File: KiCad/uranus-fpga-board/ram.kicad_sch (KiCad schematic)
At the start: 61 parts, among them U6 AS4C256M16D3, U7 AS4C256M16D3, U8 AS4C256M16D3, U9 AS4C256M16D3

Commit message: New entry and schematic
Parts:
- added Y1: SX7DF200.000B20F30DNN, Oscillator:Oscillator_SMD_IDT_JU6-6_7.0x5.0mm_P2.54mm, symbol Oscillator:XUX71
- C10: renamed from C1; value 100 nF -> 100 nF 0.1%
- C11: renamed from C2; value 100 nF -> 100 nF 0.1%
- C13: renamed from C28; value C_Small -> 100 nF
- C14: renamed from C29; value C_Small -> 100 nF
- C15: renamed from C30; value C_Small -> 100 nF
- C16: renamed from C31; value C_Small -> 100 nF
- C17: renamed from C32; value C_Small -> 100 nF
- C18: renamed from C33; value C_Small -> 100 nF
- C19: renamed from C34; value C_Small -> 100 nF
- C2: renamed from C10; value C_Small -> 100 nF
- C20: renamed from C35; value C_Small -> 100 nF
- C21: renamed from C5; value 100 nF -> 100 nF 0.1%
- C23: renamed from C19; value C_Small -> 100 nF
- C24: renamed from C20; value C_Small -> 100 nF
- C25: renamed from C21; value C_Small -> 100 nF
- C26: renamed from C22; value C_Small -> 100 nF
- C27: renamed from C23; value C_Small -> 100 nF
- C28: renamed from C24; value C_Small -> 100 nF
- C29: renamed from C25; value C_Small -> 100 nF
- C3: renamed from C11; value C_Small -> 100 nF
- C30: renamed from C26; value C_Small -> 100 nF
- C31: renamed from C6; value 100 nF -> 100 nF 0.1%
- C33: renamed from C37; value C_Small -> 100 nF
- C34: renamed from C38; value C_Small -> 100 nF
- C35: renamed from C39; value C_Small -> 100 nF
- C36: renamed from C40; value C_Small -> 100 nF
- C37: renamed from C41; value C_Small -> 100 nF
- C38: renamed from C42; value C_Small -> 100 nF
- C39: renamed from C43; value C_Small -> 100 nF
- C4: renamed from C12; value C_Small -> 100 nF
- C40: renamed from C44; value C_Small -> 100 nF
- C41: renamed from C7; value 100 nF -> 100 nF 0.1%
- C42: renamed from C8; value 100 nF -> 100 nF 0.1%
- C43: renamed from C45; value 10 uF -> 10 μF
- C44: renamed from C3; value 100 nF -> 100 nF 0.1%
- C45: renamed from C4; value 100 nF -> 100 nF 0.1%
- C5: renamed from C13; value C_Small -> 100 nF
- C6: renamed from C14; value C_Small -> 100 nF
- C7: renamed from C15; value C_Small -> 100 nF
- C8: renamed from C16; value C_Small -> 100 nF
- C9: renamed from C17; value C_Small -> 100 nF
- renumbered C9 to C1, C27 to C12, C18 to C22, C36 to C32, R12 to R10, R7 to R11, R8 to R12, R10 to R13, R1 to R2, R2 to R3, R9 to R4, R3 to R5, R4 to R6, R11 to R7, R5 to R8, R6 to R9, U6 to U2, U8 to U3, U9 to U4, U7 to U5
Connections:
- net GND: now also Y1.3 (GND)
- new net +3V3: Y1.6 (VDD)

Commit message: New journal entry, progress on schematic and PCB
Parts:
- R10, R13, R4, R7: footprint Package_DIP:DIP-8_W7.62mm -> Resistor_SMD:R_0402_1005Metric
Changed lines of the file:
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@@
 			)
 		)
-		(property "Footprint" "Package_DIP:DIP-8_W7.62mm"
+		(property "Footprint" "Resistor_SMD:R_0402_1005Metric"
 			(at 200.66 101.6 0)
 			(hide yes)
@@
 			)
 		)
-		(property "Footprint" "Package_DIP:DIP-8_W7.62mm"
+		(property "Footprint" "Resistor_SMD:R_0402_1005Metric"
 			(at 132.08 101.6 0)
 			(hide yes)
@@
 			)
 		)
-		(property "Footprint" "Package_DIP:DIP-8_W7.62mm"
+		(property "Footprint" "Resistor_SMD:R_0402_1005Metric"
 			(at 270.51 101.6 0)
 			(hide yes)
@@
 			)
 		)
-		(property "Footprint" "Package_DIP:DIP-8_W7.62mm"
+		(property "Footprint" "Resistor_SMD:R_0402_1005Metric"
 			(at 63.5 101.6 0)
 			(hide yes)

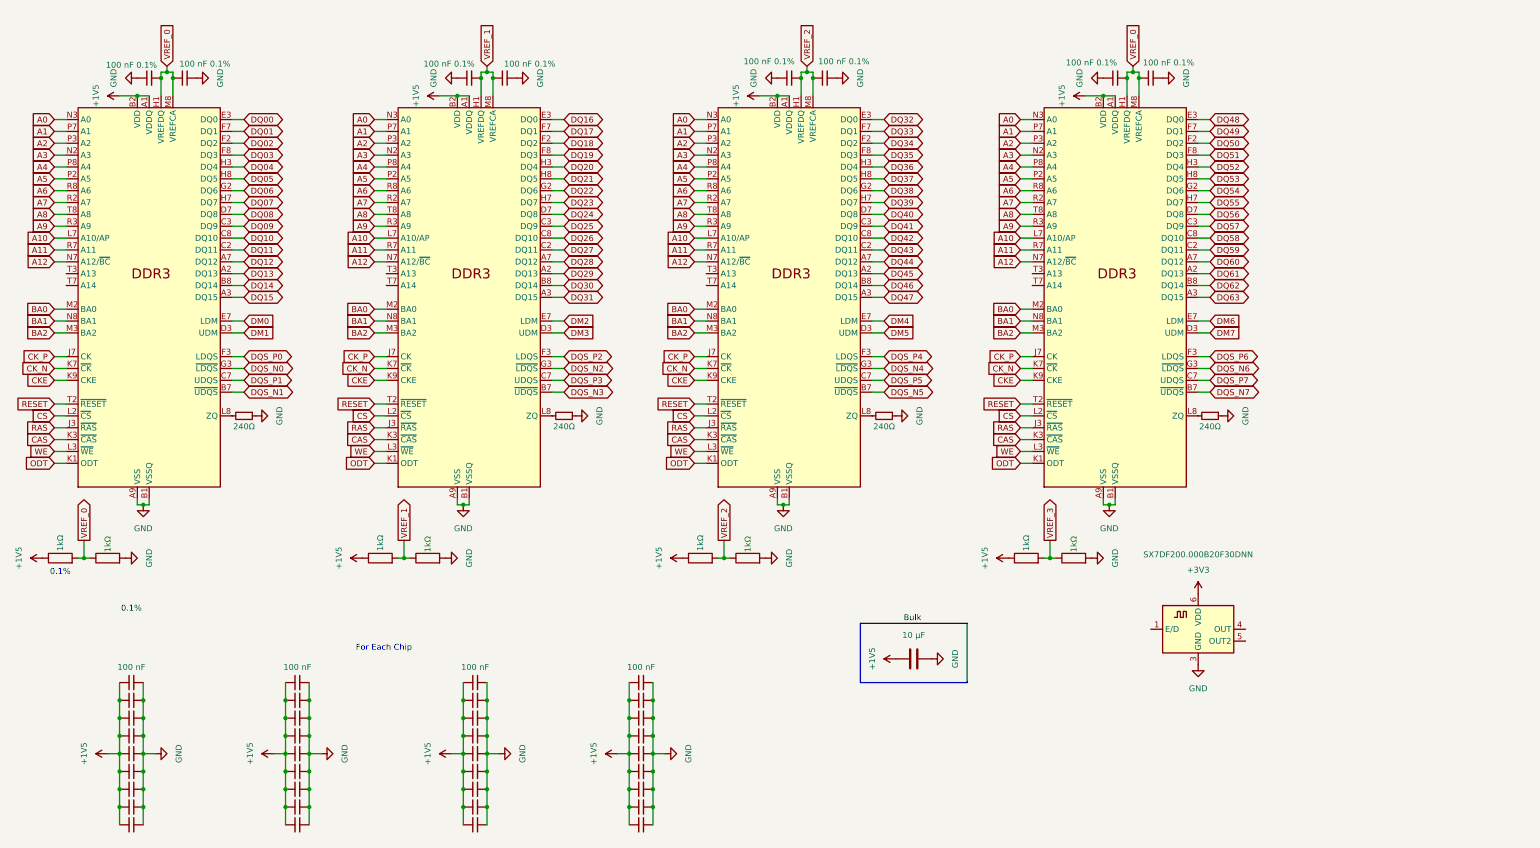
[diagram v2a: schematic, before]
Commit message: New journal, moved BOMS into a new directory
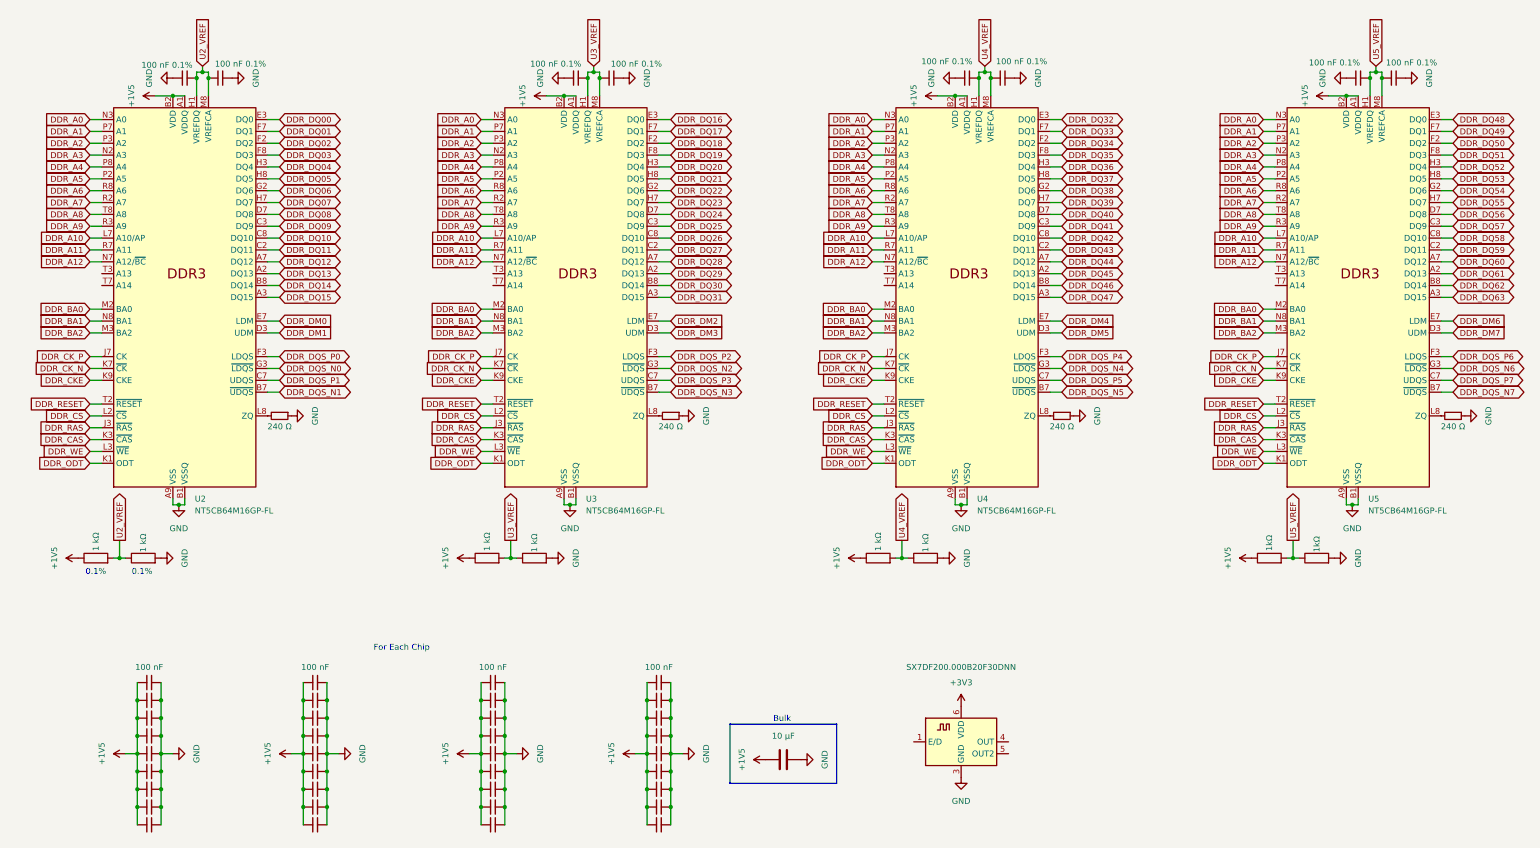
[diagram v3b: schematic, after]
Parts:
- R1: renamed from R2; value 1kΩ -> 1 kΩ
- R12: renamed from R13; value 240Ω -> 240 Ω
- R2: renamed from R3; value 1kΩ -> 1 kΩ
- R3: renamed from R4; value 240Ω -> 240 Ω
- R4: renamed from R5; value 1kΩ -> 1 kΩ
- R5: renamed from R6; value 1kΩ -> 1 kΩ
- R6: renamed from R7; value 240Ω -> 240 Ω
- R7: renamed from R8; value 1kΩ -> 1 kΩ
- R8: renamed from R9; value 1kΩ -> 1 kΩ
- R9: renamed from R10; value 240Ω -> 240 Ω
- U2, U3, U4, U5: value AS4C256M16D3 -> NT5CB64M16GP-FL
- renumbered C1 to C23, C2 to C24, C3 to C25, C4 to C26, C5 to C27, C6 to C28, C7 to C29, C8 to C30, C9 to C31, C10 to C32, C11 to C33, C12 to C34, C13 to C35, C14 to C36, C15 to C37, C16 to C38, C17 to C39, C18 to C40, C19 to C41, C20 to C42, C21 to C43, C22 to C44, C23 to C45, C24 to C46, C25 to C47, C26 to C48, C27 to C49, C28 to C50, C29 to C51, C30 to C52, C31 to C53, C32 to C54, C33 to C55, C34 to C56, C35 to C57, C36 to C58, C37 to C59, C38 to C60, C39 to C61, C40 to C62, C41 to C63, C42 to C64, C43 to C65, C44 to C66, C45 to C67, R11 to R10, R12 to R11
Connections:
- net A0 renamed DDR_A0
- net A1 renamed DDR_A1
- net A10 renamed DDR_A10
- net A11 renamed DDR_A11
- net A12 renamed DDR_A12
- net A2 renamed DDR_A2
- net A3 renamed DDR_A3
- net A4 renamed DDR_A4
- net A5 renamed DDR_A5
- net A6 renamed DDR_A6
- net A7 renamed DDR_A7
- net A8 renamed DDR_A8
- net A9 renamed DDR_A9
- net BA0 renamed DDR_BA0
- net BA1 renamed DDR_BA1
- net BA2 renamed DDR_BA2
- net CAS renamed DDR_CAS
- net CKE renamed DDR_CKE
- net CK_N renamed DDR_CK_N
- net CK_P renamed DDR_CK_P
- net CS renamed DDR_CS
- net DM0 renamed DDR_DM0
- net DM1 renamed DDR_DM1
- net DM2 renamed DDR_DM2
- net DM3 renamed DDR_DM3
- net DM4 renamed DDR_DM4
- net DM5 renamed DDR_DM5
- net DM6 renamed DDR_DM6
- net DM7 renamed DDR_DM7
- net DQ00 renamed DDR_DQ00
- net DQ01 renamed DDR_DQ01
- net DQ02 renamed DDR_DQ02
- net DQ03 renamed DDR_DQ03
- net DQ04 renamed DDR_DQ04
- net DQ05 renamed DDR_DQ05
- net DQ06 renamed DDR_DQ06
- net DQ07 renamed DDR_DQ07
- net DQ08 renamed DDR_DQ08
- net DQ09 renamed DDR_DQ09
- net DQ10 renamed DDR_DQ10
- net DQ11 renamed DDR_DQ11
- net DQ12 renamed DDR_DQ12
- net DQ13 renamed DDR_DQ13
- net DQ14 renamed DDR_DQ14
- net DQ15 renamed DDR_DQ15
- net DQ16 renamed DDR_DQ16
- net DQ17 renamed DDR_DQ17
- net DQ18 renamed DDR_DQ18
- net DQ19 renamed DDR_DQ19
- net DQ20 renamed DDR_DQ20
- net DQ21 renamed DDR_DQ21
- net DQ22 renamed DDR_DQ22
- net DQ23 renamed DDR_DQ23
- net DQ24 renamed DDR_DQ24
- net DQ25 renamed DDR_DQ25
- net DQ26 renamed DDR_DQ26
- net DQ27 renamed DDR_DQ27
- net DQ28 renamed DDR_DQ28
- net DQ29 renamed DDR_DQ29
- net DQ30 renamed DDR_DQ30
- net DQ31 renamed DDR_DQ31
- net DQ32 renamed DDR_DQ32
- net DQ33 renamed DDR_DQ33
- net DQ34 renamed DDR_DQ34
- net DQ35 renamed DDR_DQ35
- net DQ36 renamed DDR_DQ36
- net DQ37 renamed DDR_DQ37
- net DQ38 renamed DDR_DQ38
- net DQ39 renamed DDR_DQ39
- net DQ40 renamed DDR_DQ40
- net DQ41 renamed DDR_DQ41
- net DQ42 renamed DDR_DQ42
- net DQ43 renamed DDR_DQ43
- net DQ44 renamed DDR_DQ44
- net DQ45 renamed DDR_DQ45
- net DQ46 renamed DDR_DQ46
- net DQ47 renamed DDR_DQ47
- net DQ48 renamed DDR_DQ48
- net DQ49 renamed DDR_DQ49
- net DQ50 renamed DDR_DQ50
- net DQ51 renamed DDR_DQ51
- net DQ52 renamed DDR_DQ52
- net DQ53 renamed DDR_DQ53
- net DQ54 renamed DDR_DQ54
- net DQ55 renamed DDR_DQ55
- net DQ56 renamed DDR_DQ56
- net DQ57 renamed DDR_DQ57
- net DQ58 renamed DDR_DQ58
- net DQ59 renamed DDR_DQ59
- net DQ60 renamed DDR_DQ60
- net DQ61 renamed DDR_DQ61
- net DQ62 renamed DDR_DQ62
- net DQ63 renamed DDR_DQ63
- net DQS_N0 renamed DDR_DQS_N0
- net DQS_N1 renamed DDR_DQS_N1
- net DQS_N2 renamed DDR_DQS_N2
- net DQS_N3 renamed DDR_DQS_N3
- net DQS_N4 renamed DDR_DQS_N4
- net DQS_N5 renamed DDR_DQS_N5
- net DQS_N6 renamed DDR_DQS_N6
- net DQS_N7 renamed DDR_DQS_N7
- net DQS_P0 renamed DDR_DQS_P0
- net DQS_P1 renamed DDR_DQS_P1
- net DQS_P2 renamed DDR_DQS_P2
- net DQS_P3 renamed DDR_DQS_P3
- net DQS_P4 renamed DDR_DQS_P4
- net DQS_P5 renamed DDR_DQS_P5
- net DQS_P6 renamed DDR_DQS_P6
- net DQS_P7 renamed DDR_DQS_P7
- net ODT renamed DDR_ODT
- net RAS renamed DDR_RAS
- net RESET renamed DDR_RESET
- net VREF_0 renamed U2_VREF
- net U2_VREF: no longer C66.2, C67.1, U5.H1 (VREFDQ), U5.M8 (VREFCA)
- net VREF_1 renamed U3_VREF
- net VREF_2 renamed U4_VREF
- net VREF_3 renamed U5_VREF
- net U5_VREF: now also C66.2, C67.1, U5.H1 (VREFDQ), U5.M8 (VREFCA)
- net WE renamed DDR_WE

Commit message: Oct 18 journal
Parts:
- renumbered C44 to C43, C45 to C44, C46 to C45, C47 to C46, C48 to C47, C49 to C48, C50 to C49, C51 to C50, C52 to C51, C43 to C52, C65 to C63, C63 to C64, C64 to C65
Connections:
- net DDR_CAS renamed ~{DDR_CAS}
- net DDR_CS renamed ~{DDR_CS}
- net DDR_RAS renamed ~{DDR_RAS}
- net DDR_WE renamed ~{DDR_WE}

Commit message: big things happening in JOURNAL
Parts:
- removed R12, R3, R6, R9: 240 Ω, Resistor_SMD:R_0402_1005Metric, symbol Device:R_Small
- added R12, R3, R6, R9: 240 Ω, Resistor_SMD:R_0402_1005Metric, symbol Device:R
- R1, R2, R4, R5, R7, R8: footprint (none) -> Resistor_SMD:R_0402_1005Metric; MANUFACTURER (none) -> VISHAY; MP (none) -> MMA02040D1001BB300
- R10, R11: value 1kΩ -> 1 kΩ; footprint (none) -> Resistor_SMD:R_0402_1005Metric; MANUFACTURER (none) -> VISHAY; MP (none) -> MMA02040D1001BB300
- renumbered C23 to C25, C24 to C26, C25 to C27, C26 to C28, C27 to C29, C28 to C30, C29 to C31, C30 to C32, C31 to C33, C32 to C34, C33 to C35, C34 to C36, C35 to C37, C36 to C38, C37 to C39, C38 to C40, C39 to C41, C40 to C42, C41 to C43, C42 to C44, C43 to C45, C44 to C46, C45 to C47, C46 to C48, C47 to C49, C48 to C50, C49 to C51, C50 to C52, C51 to C53, C52 to C54, C53 to C55, C54 to C56, C55 to C57, C56 to C58, C57 to C59, C58 to C60, C59 to C61, C60 to C62, C61 to C63, C62 to C64, C63 to C65, C64 to C66, C65 to C67, C66 to C68, C67 to C69
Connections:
- net GND: now also R12.1, R3.1, R6.1, R9.1
- net at U2.L8 (ZQ): now also R3.2
- net at U4.L8 (ZQ): now also R9.2
- net at U3.L8 (ZQ): now also R6.2
- net at U5.L8 (ZQ): now also R12.2

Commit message: big things happening in schematic quality
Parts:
- removed C25, C26, C27, C28, C29, C30, C31, C32, C33, C36, C37, C38, C39, C40, C41, C42, C43, C44, C45, C46, C47, C48, C49, C50, C51, C52, C53, C56, C57, C58, C59, C60, C61, C62, C63, C64: 100 nF, symbol Device:C_Small
- removed C34, C35, C54, C55, C66, C67, C68, C69: 100 nF 0.1%, symbol Device:C_Small
- removed R1, R10, R11, R2, R4, R5, R7, R8: 1 kΩ, Resistor_SMD:R_0402_1005Metric, symbol Device:R
- removed R12, R3, R6, R9: 240 Ω, Resistor_SMD:R_0402_1005Metric, symbol Device:R
- removed U2, U3, U4, U5: NT5CB64M16GP-FL, Package_BGA:FBGA-96_8x13mm_Layout9x16_P0.8mm, symbol Memory_RAM:AS4C256M16D3
- removed Y1: SX7DF200.000B20F30DNN, Oscillator:Oscillator_SMD_IDT_JU6-6_7.0x5.0mm_P2.54mm, symbol Oscillator:XUX71
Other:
- added sheet Chip0 (ram_chip.kicad_sch)
- added sheet Chip1 (ram_chip.kicad_sch)
- added sheet Chip2 (ram_chip.kicad_sch)
- added sheet Chip3 (ram_chip.kicad_sch)
- note removed: "0.1%"
- note removed: "For Each Chip"
- moved on the sheet: C65

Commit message: Big things have mostly happened in schematic quality
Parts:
- renumbered C65 to C25
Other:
- moved on the sheet: C25
